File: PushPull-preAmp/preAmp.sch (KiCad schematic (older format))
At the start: 33 parts, among them P1 PWR, P2 OUT, P3 IN, U1 TL072

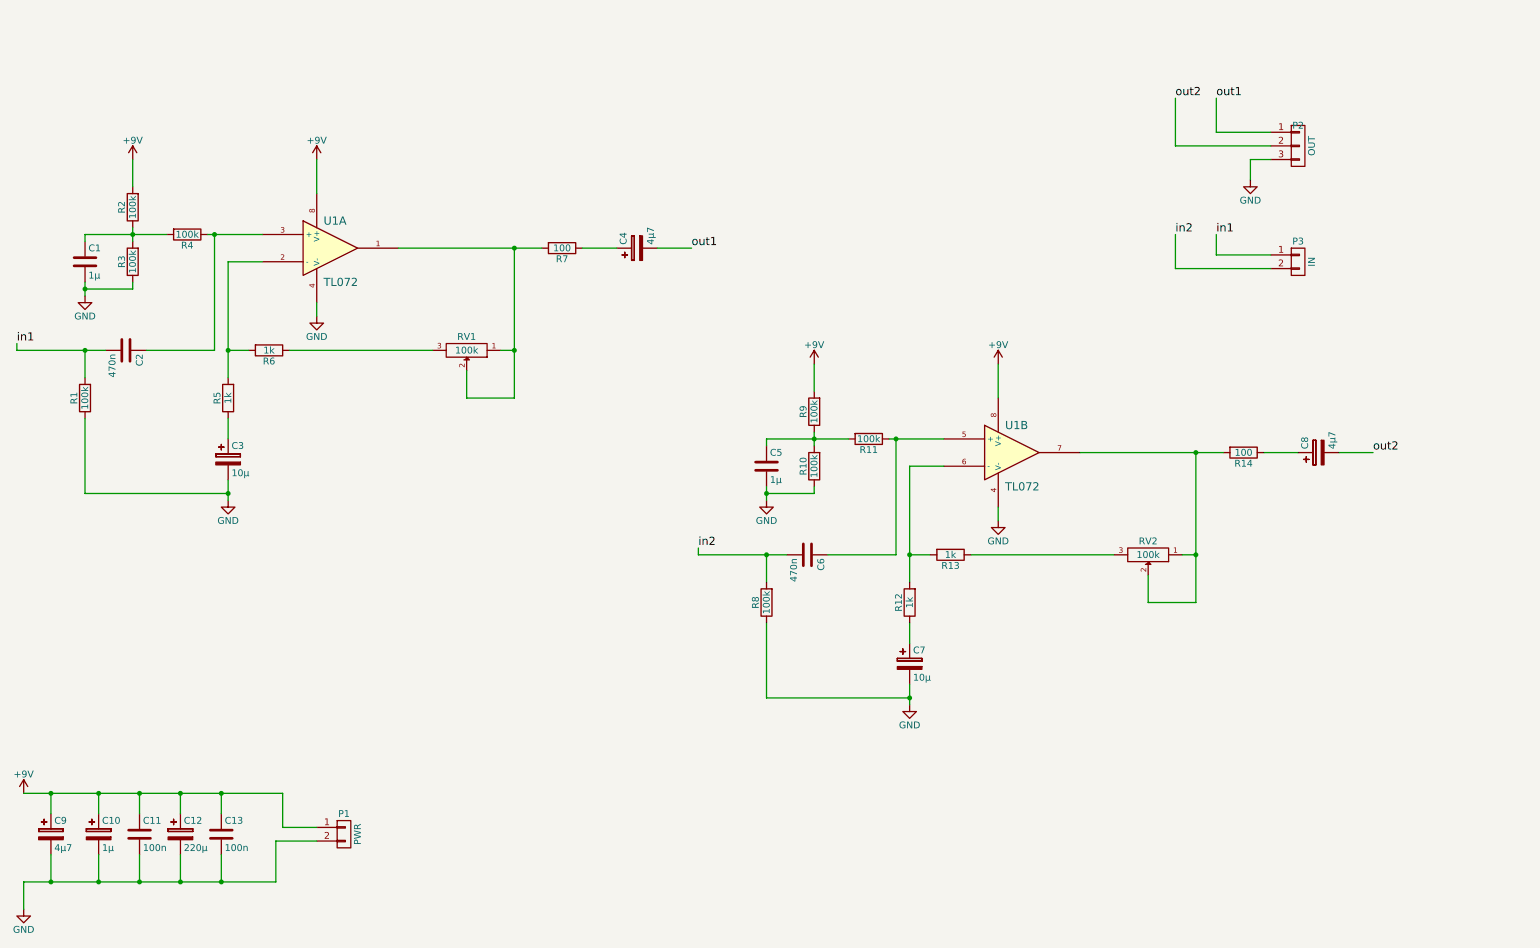
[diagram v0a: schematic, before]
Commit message: electret capsule bias, small fixes
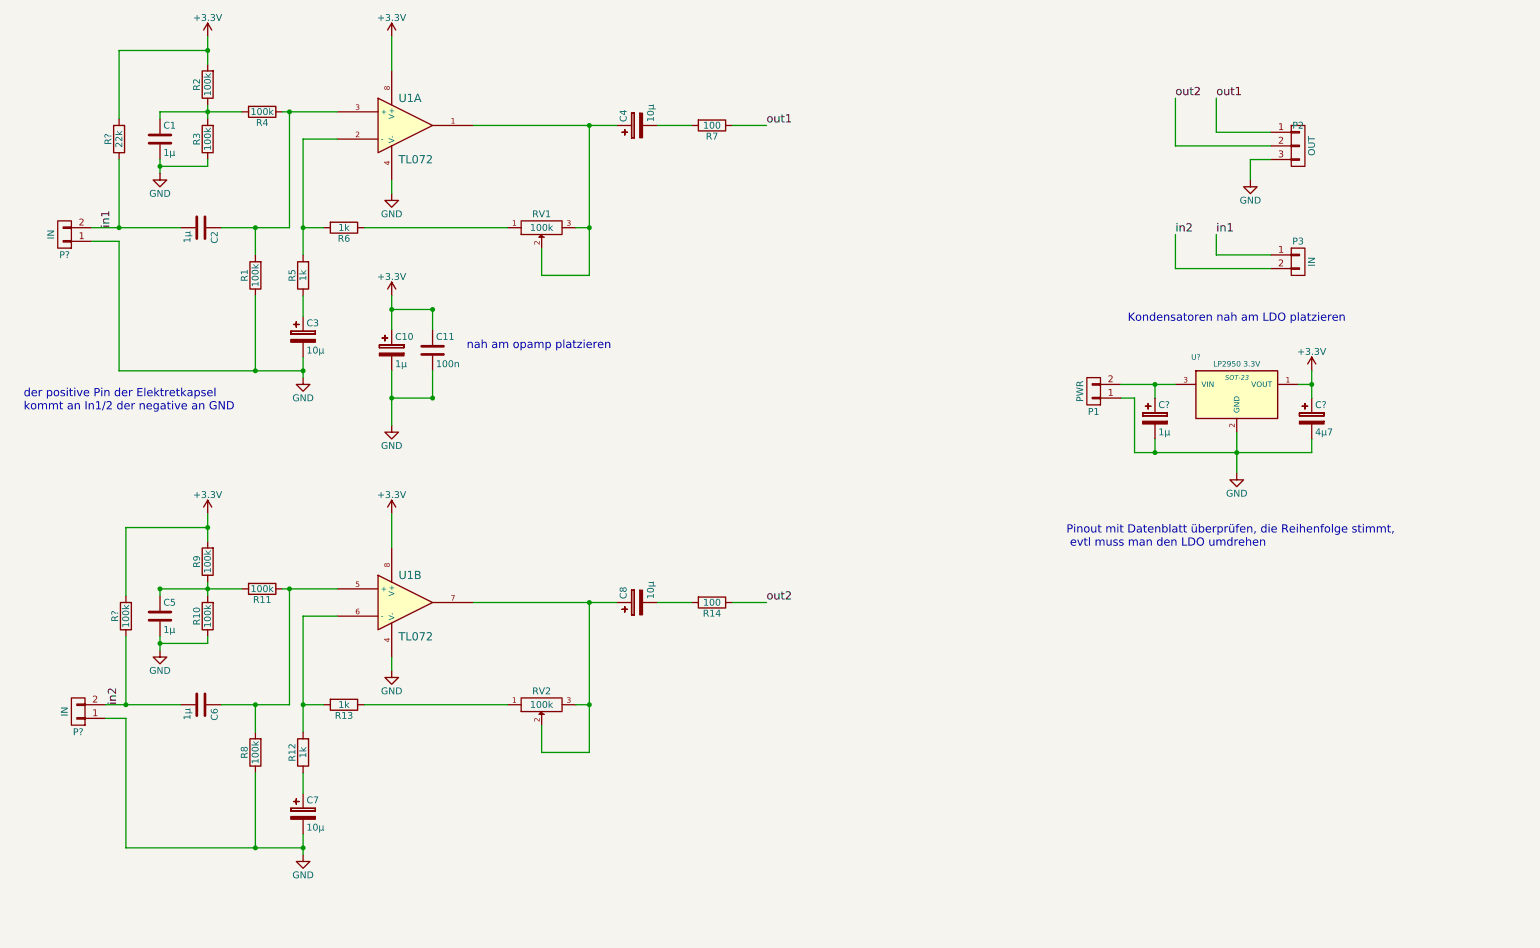
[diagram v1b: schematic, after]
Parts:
- removed C12: 220µ, Capacitors_Elko_ThroughHole:Elko_vert_11.2x6.3mm_RM2.5, symbol CP
- removed C13: 100n, Capacitors_ThroughHole:C_Rect_L4_W2.5_P2.5, symbol C
- removed C9: 4µ7, Capacitors_Elko_ThroughHole:Elko_vert_11.2x6.3mm_RM2.5, symbol CP
- added C?: 1µ, Capacitors_Elko_ThroughHole:Elko_vert_11.2x6.3mm_RM2.5, symbol CP
- added C?: 4µ7, Capacitors_Elko_ThroughHole:Elko_vert_11.2x6.3mm_RM2.5, symbol CP
- added P? (x2): IN, Pin_Headers:Pin_Header_Straight_1x02, symbol CONN_01X02
- added R?: 22k, Resistors_ThroughHole:Resistor_Horizontal_RM10mm, symbol R
- added R?: 100k, Resistors_ThroughHole:Resistor_Horizontal_RM10mm, symbol R
- added U?: LP2950 3.3V, SOT-23, symbol APE8865NL-33-HF-3
- C2, C6: value 470n -> 1µ
- C4, C8: value 4µ7 -> 10µ
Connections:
- net GND: now also P1.1 (P1), C?.2, C?.2, P?.1 (P1), P?.1 (P1), U?.2 (GND); no longer P1.2 (P2)
- net in1: now also P?.2 (P2), R?.1; no longer R1.2
- net in2: now also P?.2 (P2), R?.1; no longer R8.2
- net out1: now also R7.1; no longer C4.2
- net out2: now also R14.1; no longer C8.2
- net at C6.1, R11.1, U1.5 (+): now also R8.2
- net at RV2.2, U1.7: now also C8.1, RV2.3; no longer R14.2, RV2.1
- net at R13.1: now also RV2.1; no longer RV2.3
- net at RV1.2, U1.1: now also C4.1, RV1.3; no longer R7.2, RV1.1
- net at C2.1, R4.1, U1.3 (+): now also R1.2
- net at R6.1: now also RV1.1; no longer RV1.3
- net +9V renamed +3V3
- net +3V3: now also C?.1, R?.2, R?.2, U?.1 (VOUT); no longer P1.1 (P1)
- new net: C8.2, R14.2
- new net: C?.1, P1.2 (P2), U?.3 (VIN)
- new net: C4.2, R7.2
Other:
- note added: "Kondensatoren nah am LDO platzieren"
- note added: "Pinout mit Datenblatt überprüfen, die Reihenfolge stimmt,\n evtl muss man den LDO umdrehen"
- note added: "der positive Pin der Elektretkapsel \nkommt an In1/2 der negative an GND"
- note added: "nah am opamp platzieren"
- moved on the sheet: C1, C10, C11, C2, C3, C4, C5, C6, C7, C8, P1, R1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

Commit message: preamp layout single sided
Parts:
- C2, C6: footprint Capacitors_ThroughHole:C_Rect_L4_W2.5_P2.5 -> Capacitors_ThroughHole:C_Rect_L7_W4.5_P5
- U2: renamed from U?; footprint SOT-23 -> Discret:TO92
- gave numbers to parts that had none: 6
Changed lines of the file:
@@
 F 0 "C6" H 2075 5850 50  0000 L CNN
 F 1 "1µ" H 2075 5650 50  0000 L CNN
-F 2 "Capacitors_ThroughHole:C_Rect_L4_W2.5_P2.5" H 2088 5600 30  0001 C CNN
+F 2 "Capacitors_ThroughHole:C_Rect_L7_W4.5_P5" H 2088 5600 30  0001 C CNN
 F 3 "" H 2050 5750 60  0000 C CNN
 	1    2050 5750
@@
 $EndComp
 $Comp
-L GND #PWR06
+L GND #PWR04
 U 1 1 556AF522
 P 3450 3700
-F 0 "#PWR06" H 3450 3450 50  0001 C CNN
+F 0 "#PWR04" H 3450 3450 50  0001 C CNN
 F 1 "GND" H 3450 3550 50  0000 C CNN
 F 2 "" H 3450 3700 60  0000 C CNN
@@
 $EndComp
 $Comp
-L GND #PWR08
+L GND #PWR05
 U 1 1 556B28C5
 P 3450 2000
-F 0 "#PWR08" H 3450 1750 50  0001 C CNN
+F 0 "#PWR05" H 3450 1750 50  0001 C CNN
 F 1 "GND" H 3450 1850 50  0000 C CNN
 F 2 "" H 3450 2000 60  0000 C CNN
@@
 $EndComp
 $Comp
-L GND #PWR09
+L GND #PWR06
 U 1 1 556B28D1
 P 1750 1850
-F 0 "#PWR09" H 1750 1600 50  0001 C CNN
+F 0 "#PWR06" H 1750 1600 50  0001 C CNN
 F 1 "GND" H 1750 1700 50  0000 C CNN
 F 2 "" H 1750 1850 60  0000 C CNN
@@
 F 0 "C2" H 2075 2350 50  0000 L CNN
 F 1 "1µ" H 2075 2150 50  0000 L CNN
-F 2 "Capacitors_ThroughHole:C_Rect_L4_W2.5_P2.5" H 2088 2100 30  0001 C CNN
+F 2 "Capacitors_ThroughHole:C_Rect_L7_W4.5_P5" H 2088 2100 30  0001 C CNN
 F 3 "" H 2050 2250 60  0000 C CNN
 	1    2050 2250
@@
 $EndComp
 $Comp
-L GND #PWR010
+L GND #PWR07
 U 1 1 556B28DD
 P 2800 3350
-F 0 "#PWR010" H 2800 3100 50  0001 C CNN
+F 0 "#PWR07" H 2800 3100 50  0001 C CNN
 F 1 "GND" H 2800 3200 50  0000 C CNN
 F 2 "" H 2800 3350 60  0000 C CNN
@@
 in1
 $Comp
-L GND #PWR013
+L GND #PWR08
 U 1 1 556B4E7F
 P 9750 1900
-F 0 "#PWR013" H 9750 1650 50  0001 C CNN
+F 0 "#PWR08" H 9750 1650 50  0001 C CNN
 F 1 "GND" H 9750 1750 50  0000 C CNN
 F 2 "" H 9750 1900 60  0000 C CNN
@@
 in2
 $Comp
-L R R?
+L R R15
 U 1 1 556D99E5
 P 1450 1600
-F 0 "R?" V 1530 1600 50  0000 C CNN
+F 0 "R15" V 1530 1600 50  0000 C CNN
 F 1 "22k" V 1450 1600 50  0000 C CNN
 F 2 "Resistors_ThroughHole:Resistor_Horizontal_RM10mm" V 1380 1600 30  0001 C CNN
@@
 $EndComp
 $Comp
-L R R?
+L R R16
 U 1 1 556DA700
 P 1500 5100
-F 0 "R?" V 1580 5100 50  0000 C CNN
+F 0 "R16" V 1580 5100 50  0000 C CNN
 F 1 "100k" V 1500 5100 50  0000 C CNN
 F 2 "Resistors_ThroughHole:Resistor_Horizontal_RM10mm" V 1430 5100 30  0001 C CNN
@@
 $EndComp
 $Comp
-L +3.3V #PWR?
+L +3.3V #PWR09
 U 1 1 556DAD7D
 P 3450 850
-F 0 "#PWR?" H 3450 700 50  0001 C CNN
+F 0 "#PWR09" H 3450 700 50  0001 C CNN
 F 1 "+3.3V" H 3450 990 50  0000 C CNN
 F 2 "" H 3450 850 60  0000 C CNN
@@
 $EndComp
 $Comp
-L +3.3V #PWR?
+L +3.3V #PWR010
 U 1 1 556DAE6D
 P 2100 850
-F 0 "#PWR?" H 2100 700 50  0001 C CNN
+F 0 "#PWR010" H 2100 700 50  0001 C CNN
 F 1 "+3.3V" H 2100 990 50  0000 C CNN
 F 2 "" H 2100 850 60  0000 C CNN
@@
 $EndComp
 $Comp
-L +3.3V #PWR?
+L +3.3V #PWR011
 U 1 1 556DAF04
 P 2100 4350
-F 0 "#PWR?" H 2100 4200 50  0001 C CNN
+F 0 "#PWR011" H 2100 4200 50  0001 C CNN
 F 1 "+3.3V" H 2100 4490 50  0000 C CNN
 F 2 "" H 2100 4350 60  0000 C CNN
@@
 $EndComp
 $Comp
-L +3.3V #PWR?
+L +3.3V #PWR012
 U 1 1 556DB079
 P 3450 4350
-F 0 "#PWR?" H 3450 4200 50  0001 C CNN
+F 0 "#PWR012" H 3450 4200 50  0001 C CNN
 F 1 "+3.3V" H 3450 4490 50  0000 C CNN
 F 2 "" H 3450 4350 60  0000 C CNN
@@
 	4900 2600 4550 2600
 $Comp
-L +3.3V #PWR?
+L +3.3V #PWR013
 U 1 1 556DB7F3
 P 3450 2750
-F 0 "#PWR?" H 3450 2600 50  0001 C CNN
+F 0 "#PWR013" H 3450 2600 50  0001 C CNN
 F 1 "+3.3V" H 3450 2890 50  0000 C CNN
 F 2 "" H 3450 2750 60  0000 C CNN
@@
 $EndComp
 $Comp
-L APE8865NL-33-HF-3 U?
+L APE8865NL-33-HF-3 U2
 U 1 1 556DBFC2
 P 9650 3450
-F 0 "U?" H 9350 3700 40  0000 C CNN
+F 0 "U2" H 9350 3700 40  0000 C CNN
 F 1 "LP2950 3.3V" H 9650 3650 40  0000 C CNN
-F 2 "SOT-23" H 9650 3550 35  0000 C CIN
+F 2 "Discret:TO92" H 9650 3550 35  0000 C CIN
 F 3 "" H 9650 3450 60  0000 C CNN
 	1    9650 3450
@@
 $EndComp
 $Comp
-L CP C?
+L CP C9
 U 1 1 556DC2C0
 P 9050 3650
-F 0 "C?" H 9075 3750 50  0000 L CNN
+F 0 "C9" H 9075 3750 50  0000 L CNN
 F 1 "1µ" H 9075 3550 50  0000 L CNN
 F 2 "Capacitors_Elko_ThroughHole:Elko_vert_11.2x6.3mm_RM2.5" H 9088 3500 30  0001 C CNN
@@
 $EndComp
 $Comp
-L CP C?
+L CP C12
 U 1 1 556DC398
 P 10200 3650
-F 0 "C?" H 10225 3750 50  0000 L CNN
+F 0 "C12" H 10225 3750 50  0000 L CNN
 F 1 "4µ7" H 10225 3550 50  0000 L CNN
 F 2 "Capacitors_Elko_ThroughHole:Elko_vert_11.2x6.3mm_RM2.5" H 10238 3500 30  0001 C CNN
@@
 Connection ~ 9650 3900
 $Comp
-L GND #PWR?
+L GND #PWR014
 U 1 1 556DC754
 P 9650 4050
-F 0 "#PWR?" H 9650 3800 50  0001 C CNN
+F 0 "#PWR014" H 9650 3800 50  0001 C CNN
 F 1 "GND" H 9650 3900 50  0000 C CNN
 F 2 "" H 9650 4050 60  0000 C CNN
@@
 Connection ~ 9050 3900
 $Comp
-L +3.3V #PWR?
+L +3.3V #PWR015
 U 1 1 556DCC15
 P 10200 3300
-F 0 "#PWR?" H 10200 3150 50  0001 C CNN
+F 0 "#PWR015" H 10200 3150 50  0001 C CNN
 F 1 "+3.3V" H 10200 3440 50  0000 C CNN
 F 2 "" H 10200 3300 60  0000 C CNN
@@
 der positive Pin der Elektretkapsel \nkommt an In1/2 der negative an GND
 $Comp
-L CONN_01X02 P?
+L CONN_01X02 P4
 U 1 1 556DF9FE
 P 1050 2300
-F 0 "P?" H 1050 2450 50  0000 C CNN
+F 0 "P4" H 1050 2450 50  0000 C CNN
 F 1 "IN" V 1150 2300 50  0000 C CNN
 F 2 "Pin_Headers:Pin_Header_Straight_1x02" H 1050 2300 60  0001 C CNN
@@
 	1450 2350 1250 2350
 $Comp
-L CONN_01X02 P?
+L CONN_01X02 P5
 U 1 1 556DFE1D
 P 1150 5800
-F 0 "P?" H 1150 5950 50  0000 C CNN
+F 0 "P5" H 1150 5950 50  0000 C CNN
 F 1 "IN" V 1250 5800 50  0000 C CNN
 F 2 "Pin_Headers:Pin_Header_Straight_1x02" H 1150 5800 60  0001 C CNN

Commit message: preamp layout drills
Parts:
- removed P1: PWR, Pin_Headers:Pin_Header_Straight_1x02, symbol CONN_01X02
- removed P3: IN, Pin_Headers:Pin_Header_Straight_1x02, symbol CONN_01X02
- added P1, P3: PWR, Pin_Headers:Pin_Header_Straight_1x03, symbol CONN_01X03
- RV1, RV2: footprint Potentiometers:Potentiometer_Trimmer-Piher-PT15-h2-5_vertical -> PushPull-footprints:Trimmer_Dual
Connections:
- net GND: now also P2.1 (P1), P1.1 (P1), P3.1 (P1); no longer P2.3 (P3)
- net out1: now also P2.3 (P3); no longer P2.1 (P1)
- net at C9.1, U2.3 (VIN): now also P1.2 (P2), P3.2 (P2)
- new net TX: P1.3 (P3), P3.3 (P3)
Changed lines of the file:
@@
 F 0 "RV2" H 4550 5650 50  0000 C CNN
 F 1 "100k" H 4550 5750 50  0000 C CNN
-F 2 "Potentiometers:Potentiometer_Trimmer-Piher-PT15-h2-5_vertical" H 4550 5750 60  0001 C CNN
+F 2 "PushPull-footprints:Trimmer_Dual" H 4550 5750 60  0001 C CNN
 F 3 "" H 4550 5750 60  0000 C CNN
 	1    4550 5750
@@
 $EndComp
 $Comp
-L GND #PWR01
+L GND #PWR12
 U 1 1 556AE963
 P 3450 5500
-F 0 "#PWR01" H 3450 5250 50  0001 C CNN
+F 0 "#PWR12" H 3450 5250 50  0001 C CNN
 F 1 "GND" H 3450 5350 50  0000 C CNN
 F 2 "" H 3450 5500 60  0000 C CNN
@@
 $EndComp
 $Comp
-L GND #PWR02
+L GND #PWR2
 U 1 1 556AEE1E
 P 1750 5350
-F 0 "#PWR02" H 1750 5100 50  0001 C CNN
+F 0 "#PWR2" H 1750 5100 50  0001 C CNN
 F 1 "GND" H 1750 5200 50  0000 C CNN
 F 2 "" H 1750 5350 60  0000 C CNN
@@
 $EndComp
 $Comp
-L GND #PWR03
+L GND #PWR6
 U 1 1 556AF0C9
 P 2800 6850
-F 0 "#PWR03" H 2800 6600 50  0001 C CNN
+F 0 "#PWR6" H 2800 6600 50  0001 C CNN
 F 1 "GND" H 2800 6700 50  0000 C CNN
 F 2 "" H 2800 6850 60  0000 C CNN
@@
 $EndComp
 $Comp
-L GND #PWR04
+L GND #PWR10
 U 1 1 556AF522
 P 3450 3700
-F 0 "#PWR04" H 3450 3450 50  0001 C CNN
+F 0 "#PWR10" H 3450 3450 50  0001 C CNN
 F 1 "GND" H 3450 3550 50  0000 C CNN
 F 2 "" H 3450 3700 60  0000 C CNN
@@
 	1    3450 3700
 	1    0    0    -1
-$EndComp
-$Comp
-L CONN_01X02 P1
-U 1 1 556AF5B2
-P 8600 3450
-F 0 "P1" H 8600 3600 50  0000 C CNN
-F 1 "PWR" V 8700 3450 50  0000 C CNN
-F 2 "Pin_Headers:Pin_Header_Straight_1x02" H 8600 3450 60  0001 C CNN
-F 3 "" H 8600 3450 60  0000 C CNN
-	1    8600 3450
-	-1   0    0    1
 $EndComp
 $Comp
@@
 F 0 "RV1" H 4550 2150 50  0000 C CNN
 F 1 "100k" H 4550 2250 50  0000 C CNN
-F 2 "Potentiometers:Potentiometer_Trimmer-Piher-PT15-h2-5_vertical" H 4550 2250 60  0001 C CNN
+F 2 "PushPull-footprints:Trimmer_Dual" H 4550 2250 60  0001 C CNN
 F 3 "" H 4550 2250 60  0000 C CNN
 	1    4550 2250
@@
 $EndComp
 $Comp
-L GND #PWR05
+L GND #PWR8
 U 1 1 556B28C5
 P 3450 2000
-F 0 "#PWR05" H 3450 1750 50  0001 C CNN
+F 0 "#PWR8" H 3450 1750 50  0001 C CNN
 F 1 "GND" H 3450 1850 50  0000 C CNN
 F 2 "" H 3450 2000 60  0000 C CNN
@@
 $EndComp
 $Comp
-L GND #PWR06
+L GND #PWR1
 U 1 1 556B28D1
 P 1750 1850
-F 0 "#PWR06" H 1750 1600 50  0001 C CNN
+F 0 "#PWR1" H 1750 1600 50  0001 C CNN
 F 1 "GND" H 1750 1700 50  0000 C CNN
 F 2 "" H 1750 1850 60  0000 C CNN
@@
 $EndComp
 $Comp
-L GND #PWR07
+L GND #PWR5
 U 1 1 556B28DD
 P 2800 3350
-F 0 "#PWR07" H 2800 3100 50  0001 C CNN
+F 0 "#PWR5" H 2800 3100 50  0001 C CNN
 F 1 "GND" H 2800 3200 50  0000 C CNN
 F 2 "" H 2800 3350 60  0000 C CNN
@@
 F 3 "" H 10100 1650 60  0000 C CNN
 	1    10100 1650
-	1    0    0    -1
+	1    0    0    1
 $EndComp
 Text Label 9500 1300 0    60   ~ 0
@@
 in1
 $Comp
-L GND #PWR08
+L GND #PWR14
 U 1 1 556B4E7F
 P 9750 1900
-F 0 "#PWR08" H 9750 1650 50  0001 C CNN
+F 0 "#PWR14" H 9750 1650 50  0001 C CNN
 F 1 "GND" H 9750 1750 50  0000 C CNN
 F 2 "" H 9750 1900 60  0000 C CNN
@@
 	1    0    0    -1
 $EndComp
-$Comp
-L CONN_01X02 P3
-U 1 1 556B63FE
-P 10100 2500
-F 0 "P3" H 10100 2650 50  0000 C CNN
-F 1 "IN" V 10200 2500 50  0000 C CNN
-F 2 "Pin_Headers:Pin_Header_Straight_1x02" H 10100 2500 60  0001 C CNN
-F 3 "" H 10100 2500 60  0000 C CNN
-	1    10100 2500
-	1    0    0    -1
-$EndComp
-Text Label 9500 2300 0    60   ~ 0
-in1
-Text Label 9200 2300 0    60   ~ 0
-in2
 $Comp
 L R R15
@@
 $EndComp
 $Comp
-L +3.3V #PWR09
+L +3.3V #PWR7
 U 1 1 556DAD7D
 P 3450 850
-F 0 "#PWR09" H 3450 700 50  0001 C CNN
+F 0 "#PWR7" H 3450 700 50  0001 C CNN
 F 1 "+3.3V" H 3450 990 50  0000 C CNN
 F 2 "" H 3450 850 60  0000 C CNN
@@
 $EndComp
 $Comp
-L +3.3V #PWR010
+L +3.3V #PWR3
 U 1 1 556DAE6D
 P 2100 850
-F 0 "#PWR010" H 2100 700 50  0001 C CNN
+F 0 "#PWR3" H 2100 700 50  0001 C CNN
 F 1 "+3.3V" H 2100 990 50  0000 C CNN
 F 2 "" H 2100 850 60  0000 C CNN
@@
 $EndComp
 $Comp
-L +3.3V #PWR011
+L +3.3V #PWR4
 U 1 1 556DAF04
 P 2100 4350
-F 0 "#PWR011" H 2100 4200 50  0001 C CNN
+F 0 "#PWR4" H 2100 4200 50  0001 C CNN
 F 1 "+3.3V" H 2100 4490 50  0000 C CNN
 F 2 "" H 2100 4350 60  0000 C CNN
@@
 $EndComp
 $Comp
-L +3.3V #PWR012
+L +3.3V #PWR11
 U 1 1 556DB079
 P 3450 4350
-F 0 "#PWR012" H 3450 4200 50  0001 C CNN
+F 0 "#PWR11" H 3450 4200 50  0001 C CNN
 F 1 "+3.3V" H 3450 4490 50  0000 C CNN
 F 2 "" H 3450 4350 60  0000 C CNN
@@
 	9750 1750 9750 1900
 Wire Wire Line
-	9200 2300 9200 2550
-Wire Wire Line
-	9200 2550 9900 2550
-Wire Wire Line
-	9500 2300 9500 2450
-Wire Wire Line
-	9500 2450 9900 2450
-Wire Wire Line
 	2700 5750 2700 4900
 Connection ~ 2700 4900
@@
 	4900 2600 4550 2600
 $Comp
-L +3.3V #PWR013
+L +3.3V #PWR9
 U 1 1 556DB7F3
 P 3450 2750
-F 0 "#PWR013" H 3450 2600 50  0001 C CNN
+F 0 "#PWR9" H 3450 2600 50  0001 C CNN
 F 1 "+3.3V" H 3450 2890 50  0000 C CNN
 F 2 "" H 3450 2750 60  0000 C CNN
@@
 	9050 3800 9050 3900
 Wire Wire Line
-	8900 3900 10200 3900
+	8800 3900 10200 3900
 Wire Wire Line
 	9650 3750 9650 4050
@@
 Connection ~ 9650 3900
 $Comp
-L GND #PWR014
+L GND #PWR13
 U 1 1 556DC754
 P 9650 4050
-F 0 "#PWR014" H 9650 3800 50  0001 C CNN
+F 0 "#PWR13" H 9650 3800 50  0001 C CNN
 F 1 "GND" H 9650 3900 50  0000 C CNN
 F 2 "" H 9650 4050 60  0000 C CNN
@@
 Connection ~ 9050 3900
 $Comp
-L +3.3V #PWR015
+L +3.3V #PWR15
 U 1 1 556DCC15
 P 10200 3300
-F 0 "#PWR015" H 10200 3150 50  0001 C CNN
+F 0 "#PWR15" H 10200 3150 50  0001 C CNN
 F 1 "+3.3V" H 10200 3440 50  0000 C CNN
 F 2 "" H 10200 3300 60  0000 C CNN
@@
 Text Notes 8400 4600 0    60   ~ 0
 Pinout mit Datenblatt überprüfen, die Reihenfolge stimmt,\n evtl muss man den LDO umdrehen
+$Comp
+L CONN_01X03 P1
+U 1 1 55705D11
+P 8600 3400
+F 0 "P1" H 8600 3550 50  0000 C CNN
+F 1 "PWR" V 8700 3400 50  0000 C CNN
+F 2 "Pin_Headers:Pin_Header_Straight_1x03" H 8600 3400 60  0001 C CNN
+F 3 "" H 8600 3400 60  0000 C CNN
+	1    8600 3400
+	-1   0    0    1
+$EndComp
+Wire Wire Line
+	8800 3300 9200 3300
+Text Label 8950 3300 0    60   ~ 0
+TX
+$Comp
+L CONN_01X03 P3
+U 1 1 557060A7
+P 8600 3800
+F 0 "P3" H 8600 3950 50  0000 C CNN
+F 1 "PWR" V 8700 3800 50  0000 C CNN
+F 2 "Pin_Headers:Pin_Header_Straight_1x03" H 8600 3800 60  0001 C CNN
+F 3 "" H 8600 3800 60  0000 C CNN
+	1    8600 3800
+	-1   0    0    1
+$EndComp
+Connection ~ 8900 3900
+Wire Wire Line
+	8800 3800 8950 3800
+Wire Wire Line
+	8950 3800 8950 3400
+Connection ~ 8950 3400
+Wire Wire Line
+	8800 3700 9200 3700
+Wire Wire Line
+	9200 3700 9200 3300
 $EndSCHEMATC

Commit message: updates.
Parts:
- R16: value 100k -> 22k
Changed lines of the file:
@@
 LIBS:memory
 LIBS:xilinx
-LIBS:special
 LIBS:microcontrollers
 LIBS:dsp
@@
 P 1500 5100
 F 0 "R16" V 1580 5100 50  0000 C CNN
-F 1 "100k" V 1500 5100 50  0000 C CNN
+F 1 "22k" V 1500 5100 50  0000 C CNN
 F 2 "Resistors_ThroughHole:Resistor_Horizontal_RM10mm" V 1430 5100 30  0001 C CNN
 F 3 "" H 1500 5100 30  0000 C CNN
